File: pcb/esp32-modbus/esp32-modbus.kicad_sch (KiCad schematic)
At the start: 52 parts, among them J1 Conn_01x01_Male, J10 Conn_01x01_Male, J11 Conn_01x01_Male, J12 Conn_01x01_Male, J13 Conn_01x01_Male, J14 Conn_01x01_Male, J15 Conn_01x01_Male, J16 Conn_01x01_Male, J17 Conn_01x01_Male, J18 Conn_01x01_Male, J19 Conn_01x01_Male, J2 Conn_01x05_Male, J20 Conn_01x01_Male, J21 Conn_01x01_Male, J22 Conn_01x01_Male, J23 Conn_01x01_Male, J24 Conn_01x01_Male, J25 Conn_01x01_Male, J26 Conn_01x01_Male, J27_VCC1 Conn_01x01_Male, J28_RO1 Conn_01x01_Male, J29_DI1 Conn_01x01_Male, J3 Conn_01x01_Male, J30_RE/DE1 Conn_01x01_Male, J31_GND1 Conn_01x01_Male, J4 Conn_01x01_Male, J5 Conn_01x01_Male, J6 Screw_Terminal_01x02, J8 Conn_01x01_Male, J9 Conn_01x01_Male, Q1 2N3055, Q2 2N3055, U1 ESP32-WROOM-32U

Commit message: full prototype
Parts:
- removed J11, J14, J16, J18, J20: Conn_01x01_Male, Connector_PinHeader_1.00mm:PinHeader_1x01_P1.00mm_Vertical, symbol Connector:Conn_01x01_Male
- removed J15, J17, J19, J21, J8: Conn_01x01_Male, Connector_PinHeader_1.00mm:PinHeader_1x01_P1.00mm_Horizontal, symbol Connector:Conn_01x01_Male
- removed Q1, Q2: 2N3055, Package_TO_SOT_SMD:SOT-23W_Handsoldering, symbol Transistor_BJT:2N3055
- added D5, D6, D7, D8: LED, LED_SMD:LED_1206_3216Metric_ReverseMount_Hole1.8x2.4mm, symbol Device:LED
- added J7: Conn_01x09_Male, Connector_PinHeader_2.54mm:PinHeader_1x09_P2.54mm_Vertical, symbol Connector:Conn_01x09_Male
- added J8: Conn_01x09_Male, Connector_PinHeader_2.54mm:PinHeader_1x09_P2.54mm_Horizontal, symbol Connector:Conn_01x09_Male
- added JP4, JP5: SolderJumper_2_Open, Jumper:SolderJumper-2_P1.3mm_Open_Pad1.0x1.5mm, symbol Jumper:SolderJumper_2_Open
- added Q1, Q2: BC817, Package_TO_SOT_SMD:SOT-23, symbol Transistor_BJT:BC817
- added R2.5k5, R2.5k6, R2.5k7, R2.5k8: R, Resistor_SMD:R_0805_2012Metric_Pad1.20x1.40mm_HandSolder, symbol Device:R
- J1, J3, J4, J5: footprint Connector_PinHeader_1.00mm:PinHeader_1x01_P1.00mm_Vertical -> Connector_PinHeader_2.54mm:PinHeader_1x01_P2.54mm_Vertical
- J2: footprint Connector_PinHeader_2.00mm:PinHeader_1x05_P2.00mm_Vertical -> Connector_PinHeader_2.54mm:PinHeader_1x05_P2.54mm_Vertical
- J22, J23, J24, J25, J26, J27_VCC1, J28_RO1, J29_DI1, J30_RE/DE1, J31_GND1: footprint custom:TestPoint_Pad_4.0x4.0mm -> custom:TestPoint_Pad_4.0x4.0mm2
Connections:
- net EN: now also JP4.2 (B)
- net GND: now also J8.9 (Pin_9)
- net GPIO0: now also JP5.2 (B)
- net at R2.5k4.2: now also J8.5 (Pin_5)
- net at J1.1 (Pin_1), R10k2.1: now also Q2.2 (E)
- net at R10k2.2: now also Q1.1 (B)
- net at R2.5k3.2: now also J8.6 (Pin_6)
- net at J3.1 (Pin_1), R10k3.1: now also Q1.2 (E)
- net at D2.2 (A): now also J7.4 (Pin_4)
- net at D1.2 (A): now also J7.3 (Pin_3)
- net at R2.5k1.2: now also J8.8 (Pin_8)
- net at R2.5k2.2: now also J8.7 (Pin_7)
- net at D1.1 (K), D2.1 (K), D3.1 (K)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: now also D5.1 (K), D6.1 (K), D7.1 (K), D8.1 (K), J7.1 (Pin_1)
- net at D3.2 (A): now also J7.5 (Pin_5)
- net at R10k3.2: now also Q2.1 (B)
- net at D4.2 (A): now also J7.2 (Pin_2)
- net GPIO25: now reaches U1.10 (IO25)
- net GPIO25: now also R2.5k5.1
- net GPIO26: now reaches U1.11 (IO26)
- net GPIO26: now also R2.5k6.1
- net GPIO27: now reaches U1.12 (IO27)
- net GPIO27: now also R2.5k7.1
- net GPIO33: now reaches U1.9 (IO33)
- net GPIO33: now also R2.5k8.1
- new net: J8.1 (Pin_1), R2.5k8.2
- new net: D6.2 (A), J7.7 (Pin_7)
- new net: JP5.1 (A), Q2.3 (C)
- new net: J8.2 (Pin_2), R2.5k7.2
- new net: J8.3 (Pin_3), R2.5k6.2
- new net: J8.4 (Pin_4), R2.5k5.2
- new net: D8.2 (A), J7.9 (Pin_9)
- new net: JP4.1 (A), Q1.3 (C)
- new net: D5.2 (A), J7.6 (Pin_6)
- new net: D7.2 (A), J7.8 (Pin_8)
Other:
- note added: "Upper pcb - gpio signal light"
- note added: "| | | |"
- moved on the sheet: R2.5k1, R2.5k2, R2.5k3, R2.5k4

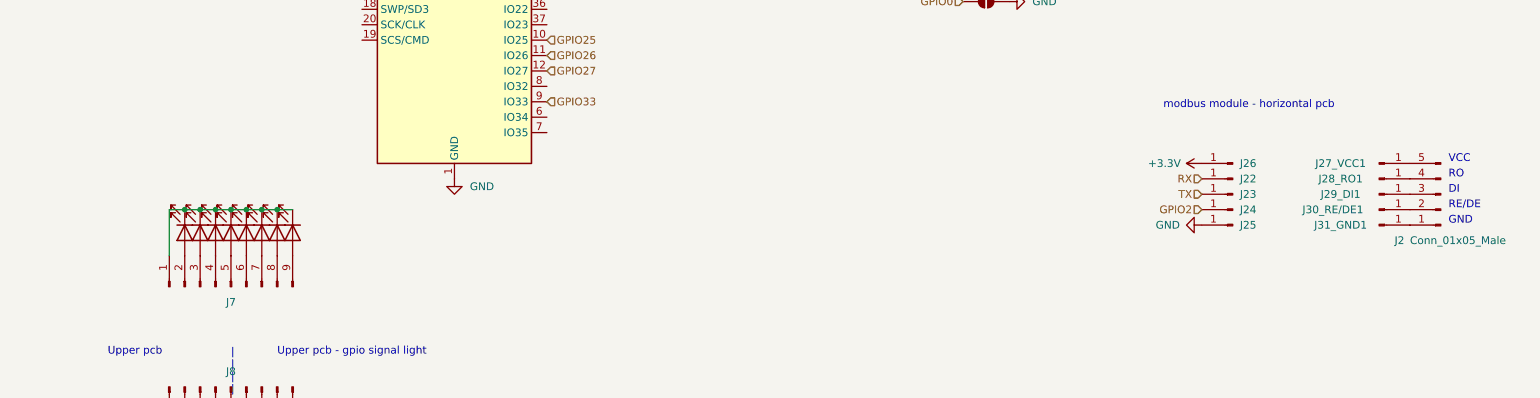
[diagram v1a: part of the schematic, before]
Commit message: pcb update, esp01 wifi
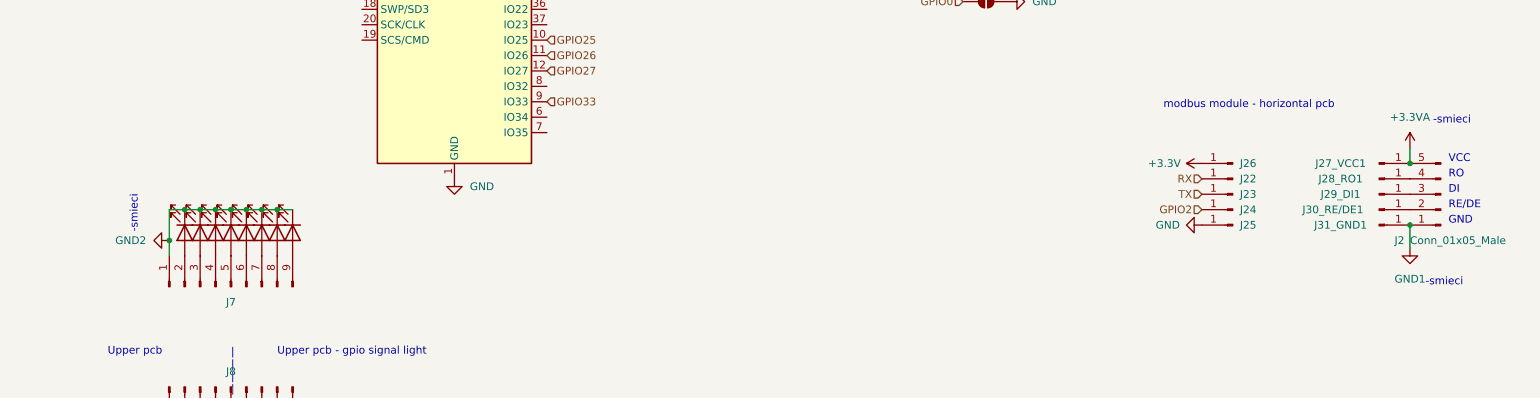
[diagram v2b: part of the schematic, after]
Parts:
- J8: footprint Connector_PinHeader_2.54mm:PinHeader_1x09_P2.54mm_Horizontal -> custom:PinHeader_1x09_P2.54mm_Horizontal
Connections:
- net GND2: now reaches D1.1 (K), D2.1 (K), D3.1 (K), D4.1 (K), D5.1 (K), D6.1 (K), D7.1 (K), D8.1 (K), J7.1 (Pin_1)
- net GND1: now reaches J2.1 (Pin_1), J31_GND1.1 (Pin_1)
- net +3.3VA: now reaches J2.5 (Pin_5), J27_VCC1.1 (Pin_1)
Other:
- note added: "-smieci"
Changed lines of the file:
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@@
   (junction (at 184.15 36.83) (diameter 0) (color 0 0 0 0)
   )
+  (junction (at 52.07 137.16) (diameter 0) (color 0 0 0 0)
+  )
   (junction (at 106.68 38.1) (diameter 0) (color 0 0 0 0)
   )
+  (junction (at 256.54 134.62) (diameter 0) (color 0 0 0 0)
+  )
   (junction (at 86.36 38.1) (diameter 0) (color 0 0 0 0)
   )
@@
   )
   (junction (at 62.23 132.08) (diameter 0) (color 0 0 0 0)
+  )
+  (junction (at 256.54 124.46) (diameter 0) (color 0 0 0 0)
   )
   (junction (at 57.15 132.08) (diameter 0) (color 0 0 0 0)
@@
     (stroke (width 0) (type default) (color 0 0 0 0))
   )
-  (wire (pts (xy 52.07 132.08) (xy 52.07 139.7))
+  (wire (pts (xy 52.07 132.08) (xy 52.07 137.16))
     (stroke (width 0) (type default) (color 0 0 0 0))
   )
@@
     (stroke (width 0) (type default) (color 0 0 0 0))
   )
+  (wire (pts (xy 52.07 137.16) (xy 52.07 139.7))
+    (stroke (width 0) (type default) (color 0 0 0 0))
+  )
   (wire (pts (xy 86.36 30.48) (xy 83.82 30.48))
     (stroke (width 0) (type default) (color 0 0 0 0))
@@
     (stroke (width 0) (type default) (color 0 0 0 0))
   )
+  (wire (pts (xy 256.54 138.43) (xy 256.54 134.62))
+    (stroke (width 0) (type default) (color 0 0 0 0))
+  )
   (wire (pts (xy 167.64 36.83) (xy 184.15 36.83))
     (stroke (width 0) (type default) (color 0 0 0 0))
@@
   )
   (wire (pts (xy 184.15 39.37) (xy 184.15 48.26))
+    (stroke (width 0) (type default) (color 0 0 0 0))
+  )
+  (wire (pts (xy 256.54 121.92) (xy 256.54 124.46))
     (stroke (width 0) (type default) (color 0 0 0 0))
   )
@@
     (effects (font (size 1.27 1.27)) (justify left bottom))
   )
+  (text "-smieci" (at 46.99 135.89 90)
+    (effects (font (size 1.27 1.27)) (justify left bottom))
+  )
+  (text "-smieci" (at 259.08 144.78 0)
+    (effects (font (size 1.27 1.27)) (justify left bottom))
+  )
   (text "DI" (at 262.89 129.54 0)
     (effects (font (size 1.27 1.27)) (justify left bottom))
@@
   )
   (text "GND" (at 262.89 134.62 0)
+    (effects (font (size 1.27 1.27)) (justify left bottom))
+  )
+  (text "-smieci" (at 260.35 118.11 0)
     (effects (font (size 1.27 1.27)) (justify left bottom))
   )
@@
     (pin "2")
   )
+  (symbol (lib_id "power:GND2") (at 52.07 137.16 270) (unit 1)
+    (in_bom yes) (on_board yes) (fields_autoplaced)
+    (property "Reference" "#PWR0114" (id 0) (at 45.72 137.16 0)
+      (effects (font (size 1.27 1.27)) hide)
+    )
+    (property "Value" "GND2" (id 1) (at 48.26 137.1599 90)
+      (effects (font (size 1.27 1.27)) (justify right))
+    )
+    (property "Footprint" "" (id 2) (at 52.07 137.16 0)
+      (effects (font (size 1.27 1.27)) hide)
+    )
+    (property "Datasheet" "" (id 3) (at 52.07 137.16 0)
+      (effects (font (size 1.27 1.27)) hide)
+    )
+    (pin "1")
+  )
   (symbol (lib_id "Connector:Conn_01x01_Male") (at 251.46 127 0) (unit 1)
     (in_bom yes) (on_board yes)
@@
       (effects (font (size 1.27 1.27)) hide)
     )
-    (property "Footprint" "Connector_PinHeader_2.54mm:PinHeader_1x09_P2.54mm_Horizontal" (id 2) (at 62.23 161.29 0)
+    (property "Footprint" "custom:PinHeader_1x09_P2.54mm_Horizontal" (id 2) (at 62.23 161.29 0)
       (effects (font (size 1.27 1.27)) hide)
     )
@@
     (pin "3")
   )
+  (symbol (lib_id "power:+3.3VA") (at 256.54 121.92 0) (unit 1)
+    (in_bom yes) (on_board yes) (fields_autoplaced)
+    (property "Reference" "#PWR0112" (id 0) (at 256.54 125.73 0)
+      (effects (font (size 1.27 1.27)) hide)
+    )
+    (property "Value" "+3.3VA" (id 1) (at 256.54 116.84 0))
+    (property "Footprint" "" (id 2) (at 256.54 121.92 0)
+      (effects (font (size 1.27 1.27)) hide)
+    )
+    (property "Datasheet" "" (id 3) (at 256.54 121.92 0)
+      (effects (font (size 1.27 1.27)) hide)
+    )
+    (pin "1")
+  )
+  (symbol (lib_id "power:GND1") (at 256.54 138.43 0) (unit 1)
+    (in_bom yes) (on_board yes) (fields_autoplaced)
+    (property "Reference" "#PWR0113" (id 0) (at 256.54 144.78 0)
+      (effects (font (size 1.27 1.27)) hide)
+    )
+    (property "Value" "GND1" (id 1) (at 256.54 143.51 0))
+    (property "Footprint" "" (id 2) (at 256.54 138.43 0)
+      (effects (font (size 1.27 1.27)) hide)
+    )
+    (property "Datasheet" "" (id 3) (at 256.54 138.43 0)
+      (effects (font (size 1.27 1.27)) hide)
+    )
+    (pin "1")
+  )
   (sheet_instances
     (path "/" (page "1"))
@@
       (reference "#PWR0111") (unit 1) (value "+3.3V") (footprint "")
     )
+    (path "/ff4caad4-5ff4-45d7-817c-110a74dff2e0"
+      (reference "#PWR0112") (unit 1) (value "+3.3VA") (footprint "")
+    )
+    (path "/ff983b83-463a-412f-9ead-a9c5500c6108"
+      (reference "#PWR0113") (unit 1) (value "GND1") (footprint "")
+    )
+    (path "/5c15a16c-c97a-4d35-9ace-8136cfb50169"
+      (reference "#PWR0114") (unit 1) (value "GND2") (footprint "")
+    )
     (path "/857e50c3-8ed0-4fe1-90fa-73c48860dd91"
       (reference "C1") (unit 1) (value "C") (footprint "Capacitor_SMD:C_0805_2012Metric_Pad1.18x1.45mm_HandSolder")
@@
     )
     (path "/693582e0-c253-4a52-9fd0-d981e289f79d"
-      (reference "J8") (unit 1) (value "Conn_01x09_Male") (footprint "Connector_PinHeader_2.54mm:PinHeader_1x09_P2.54mm_Horizontal")
+      (reference "J8") (unit 1) (value "Conn_01x09_Male") (footprint "custom:PinHeader_1x09_P2.54mm_Horizontal")
     )
     (path "/b04e2ad9-e066-4330-a1cd-c85f1b7cc3c4"

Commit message: update
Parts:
- J7: footprint Connector_PinHeader_2.54mm:PinHeader_1x09_P2.54mm_Vertical -> Connector_PinSocket_2.54mm:PinSocket_1x09_P2.54mm_Vertical
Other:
- note added: "- this is a female connector now"
- note added: "DTR"
- note added: "RTS"
- note added: "https://dl.espressif.com/dl/schematics/esp32_devkitc_v4-sch.pdf"
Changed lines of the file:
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@@
+    (effects (font (size 1.27 1.27)) (justify left bottom))
+  )
+  (text "RTS" (at 156.21 40.64 0)
     (effects (font (size 1.27 1.27)) (justify left bottom))
   )
@@
     (effects (font (size 1.27 1.27)) (justify left bottom))
   )
+  (text "DTR" (at 156.21 38.1 0)
+    (effects (font (size 1.27 1.27)) (justify left bottom))
+  )
   (text "RE/DE" (at 262.89 132.08 0)
     (effects (font (size 1.27 1.27)) (justify left bottom))
   )
+  (text "- this is a female connector now" (at 74.93 142.24 0)
+    (effects (font (size 1.27 1.27)) (justify left bottom))
+  )
   (text "GND" (at 262.89 134.62 0)
+    (effects (font (size 1.27 1.27)) (justify left bottom))
+  )
+  (text "https://dl.espressif.com/dl/schematics/esp32_devkitc_v4-sch.pdf"
+    (at 166.37 20.32 0)
     (effects (font (size 1.27 1.27)) (justify left bottom))
   )
@@
       (effects (font (size 1.27 1.27)) hide)
     )
-    (property "Footprint" "Connector_PinHeader_2.54mm:PinHeader_1x09_P2.54mm_Vertical" (id 2) (at 62.23 144.78 0)
+    (property "Footprint" "Connector_PinSocket_2.54mm:PinSocket_1x09_P2.54mm_Vertical" (id 2) (at 62.23 144.78 0)
       (effects (font (size 1.27 1.27)) hide)
     )
@@
     )
     (path "/b6892ed4-2299-4b13-8497-f98d3ae09652"
-      (reference "J7") (unit 1) (value "Conn_01x09_Male") (footprint "Connector_PinHeader_2.54mm:PinHeader_1x09_P2.54mm_Vertical")
+      (reference "J7") (unit 1) (value "Conn_01x09_Male") (footprint "Connector_PinSocket_2.54mm:PinSocket_1x09_P2.54mm_Vertical")
     )
     (path "/693582e0-c253-4a52-9fd0-d981e289f79d"
